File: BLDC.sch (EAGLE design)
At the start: 124 parts, among them J2 1729157, J3 1729128, Q1 IRFS7530TRLPBF, Q2 IRFS7530TRLPBF, Q3 IRFS7530TRLPBF, Q4 IRFS7530TRLPBF, Q5 IRFS7530TRLPBF, Q6 IRFS7530TRLPBF, U1 DRV8302, U102 LM3671MF-3.3/NOPB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

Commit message: Merge remote-tracking branch 'refs/remotes/origin/master'
Conflicts:
	BLDC.brd
	BLDC.sch
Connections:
- new net AGND: JP1.SHIELD
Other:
- note added: "Connect shield GND to signal GNN in one place only"
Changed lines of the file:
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@@
 <part name="P+4" library="supply1" deviceset="VCC" device=""/>
 <part name="P+5" library="supply1" deviceset="VCC" device=""/>
-<part name="GND17" library="supply1" deviceset="GND" device=""/>
 <part name="C27" library="rcl" deviceset="C-US" device="C0805" value="10uf, 50V">
 <attribute name="PARTNO" value="GRM21BR61E106KA73L"/>
@@
 <part name="GND36" library="supply1" deviceset="GND" device=""/>
 <part name="P+12" library="supply1" deviceset="+5V" device=""/>
+<part name="AGND1" library="supply1" deviceset="AGND" device=""/>
+<part name="AGND2" library="supply1" deviceset="AGND" device=""/>
+<part name="GND17" library="supply1" deviceset="GND" device=""/>
+<part name="SUPPLY1" library="supply2" deviceset="DGND" device=""/>
+<part name="SUPPLY2" library="supply2" deviceset="DGND" device=""/>
 </parts>
 <sheets>
@@
 <text x="-231.14" y="43.18" size="1.778" layer="97">INPUTS</text>
 <text x="-375.92" y="149.86" size="1.778" layer="97">USB shield?</text>
-<text x="-170.18" y="53.34" size="2.54" layer="97">USB shield?</text>
 <text x="-127" y="60.96" size="1.778" layer="97">Mount if used
 as USB Host</text>
@@
 <wire x1="43.18" y1="-241.3" x2="-106.68" y2="-241.3" width="0.6096" layer="97"/>
 <wire x1="-106.68" y1="-241.3" x2="-106.68" y2="-144.78" width="0.6096" layer="97"/>
+<text x="-177.8" y="45.72" size="1.778" layer="97">Connect shield
+GND to signal
+GNN in one
+place only</text>
 </plain>
 <instances>
@@
 <instance part="P+4" gate="VCC" x="-215.9" y="27.94" rot="R270"/>
 <instance part="P+5" gate="VCC" x="223.52" y="76.2"/>
-<instance part="GND17" gate="1" x="-215.9" y="25.4" rot="MR270"/>
 <instance part="C27" gate="G$1" x="236.22" y="66.04" rot="MR0">
 <attribute name="PARTNO" x="236.22" y="66.04" size="6.4516" layer="96" rot="MR0" display="off"/>
@@
 <instance part="GND36" gate="1" x="35.56" y="-190.5"/>
 <instance part="P+12" gate="1" x="35.56" y="-160.02"/>
+<instance part="AGND1" gate="VR1" x="-157.48" y="43.18"/>
+<instance part="AGND2" gate="VR1" x="-193.04" y="33.02"/>
+<instance part="GND17" gate="1" x="-185.42" y="33.02"/>
+<instance part="SUPPLY1" gate="G$1" x="-203.2" y="33.02"/>
+<instance part="SUPPLY2" gate="G$1" x="-215.9" y="25.4" rot="R90"/>
 </instances>
 <busses>
@@
 <wire x1="-76.2" y1="83.82" x2="-76.2" y2="81.28" width="0.1524" layer="91"/>
 <junction x="-76.2" y="81.28"/>
-</segment>
-<segment>
-<wire x1="-233.68" y1="25.4" x2="-218.44" y2="25.4" width="0.1524" layer="91"/>
-<label x="-233.68" y="25.4" size="1.778" layer="95"/>
-<pinref part="GND17" gate="1" pin="GND"/>
 </segment>
 <segment>
@@
 <segment>
 <pinref part="R4" gate="G$1" pin="1"/>
-<wire x1="-116.84" y1="45.72" x2="-104.14" y2="45.72" width="0.1524" layer="91"/>
-<label x="-114.3" y="45.72" size="1.778" layer="95"/>
+<wire x1="-116.84" y1="45.72" x2="-114.3" y2="45.72" width="0.1524" layer="91"/>
+<label x="-114.3" y="45.72" size="1.778" layer="95" xref="yes"/>
 </segment>
 </net>
@@
 <segment>
 <pinref part="R3" gate="G$1" pin="1"/>
-<wire x1="-116.84" y1="53.34" x2="-104.14" y2="53.34" width="0.1524" layer="91"/>
-<label x="-114.3" y="53.34" size="1.778" layer="95"/>
+<wire x1="-116.84" y1="53.34" x2="-114.3" y2="53.34" width="0.1524" layer="91"/>
+<label x="-114.3" y="53.34" size="1.778" layer="95" xref="yes"/>
 </segment>
 </net>
@@
 </segment>
 </net>
+<net name="AGND" class="0">
+<segment>
+<pinref part="JP1" gate="G$1" pin="SHIELD"/>
+<pinref part="AGND1" gate="VR1" pin="AGND"/>
+<wire x1="-152.4" y1="50.8" x2="-157.48" y2="50.8" width="0.1524" layer="91"/>
+<wire x1="-157.48" y1="50.8" x2="-157.48" y2="45.72" width="0.1524" layer="91"/>
+</segment>
+</net>
+<net name="DGND" class="0">
+<segment>
+<wire x1="-203.2" y1="35.56" x2="-203.2" y2="38.1" width="0.1524" layer="91"/>
+<pinref part="GND17" gate="1" pin="GND"/>
+<wire x1="-203.2" y1="38.1" x2="-193.04" y2="38.1" width="0.1524" layer="91"/>
+<wire x1="-193.04" y1="38.1" x2="-185.42" y2="38.1" width="0.1524" layer="91"/>
+<wire x1="-185.42" y1="38.1" x2="-185.42" y2="35.56" width="0.1524" layer="91"/>
+<pinref part="AGND2" gate="VR1" pin="AGND"/>
+<wire x1="-193.04" y1="35.56" x2="-193.04" y2="38.1" width="0.1524" layer="91"/>
+<junction x="-193.04" y="38.1"/>
+<pinref part="SUPPLY1" gate="G$1" pin="DGND"/>
+</segment>
+<segment>
+<wire x1="-233.68" y1="25.4" x2="-218.44" y2="25.4" width="0.1524" layer="91"/>
+<label x="-233.68" y="25.4" size="1.778" layer="95"/>
+<pinref part="SUPPLY2" gate="G$1" pin="DGND"/>
+</segment>
+</net>

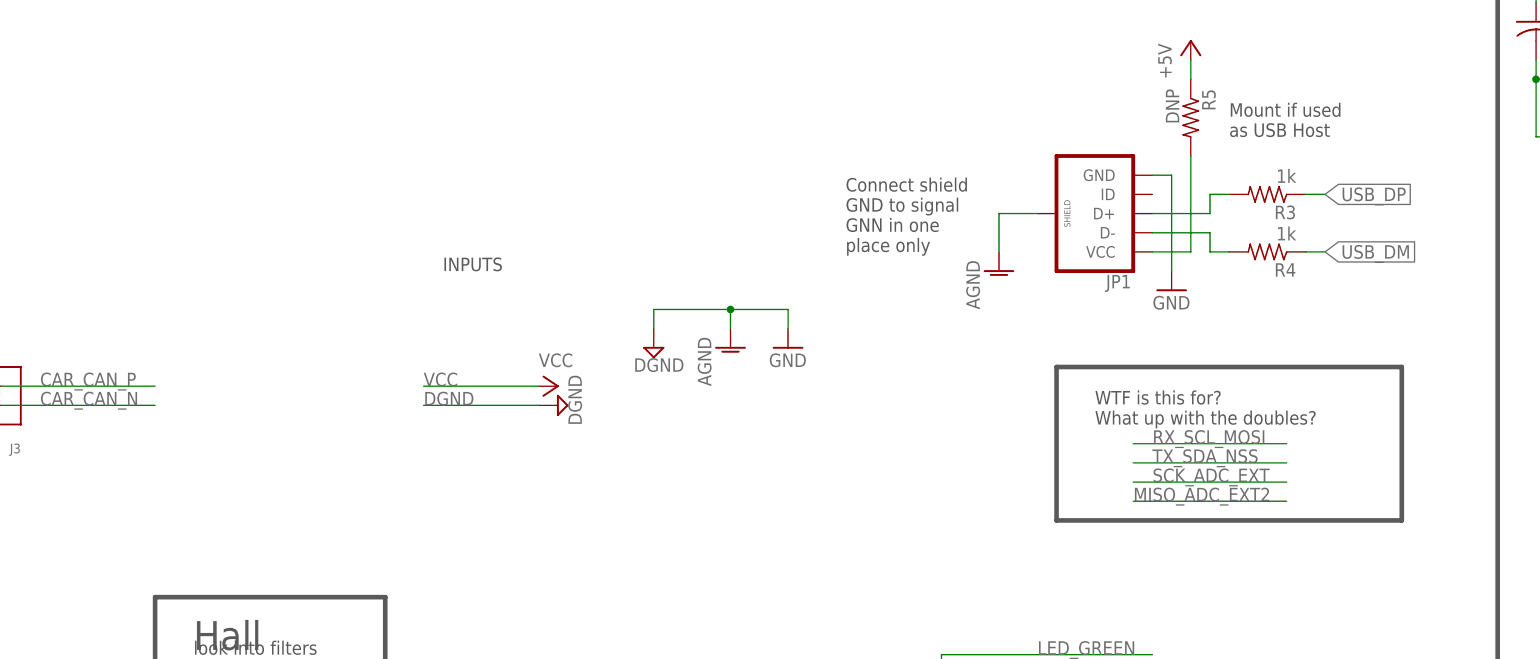
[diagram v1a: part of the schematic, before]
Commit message: added some inputs
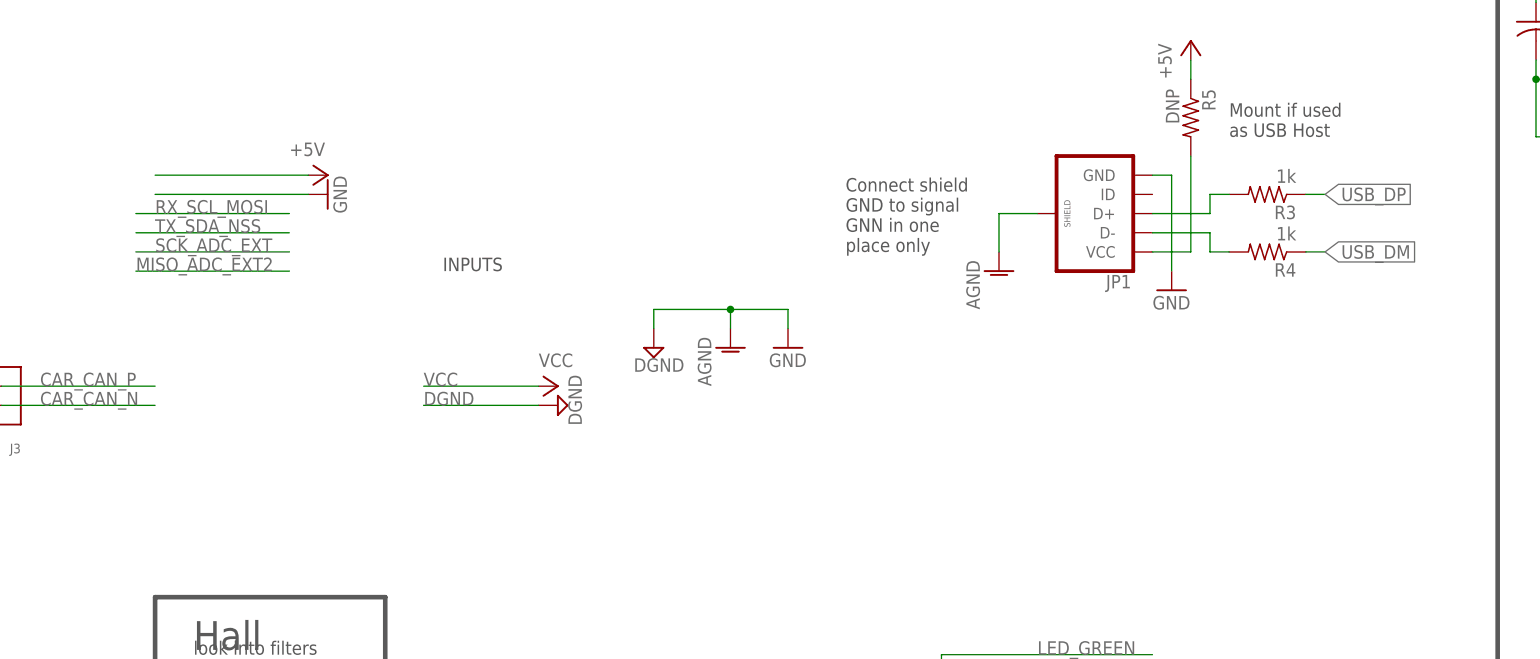
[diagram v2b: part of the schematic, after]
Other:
- note removed: "WTF is this for? What up with the doubles?"
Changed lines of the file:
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@@
 <part name="SUPPLY1" library="supply2" deviceset="DGND" device=""/>
 <part name="SUPPLY2" library="supply2" deviceset="DGND" device=""/>
+<part name="GND37" library="supply1" deviceset="GND" device=""/>
+<part name="P+13" library="supply1" deviceset="+5V" device=""/>
 </parts>
 <sheets>
@@
 Halls?</text>
 <text x="-261.62" y="203.2" size="6.4516" layer="97">BLDC-PCB</text>
-<text x="-144.78" y="22.86" size="1.778" layer="97">WTF is this for?
-What up with the doubles?</text>
-<wire x1="-149.86" y1="10.16" x2="-104.14" y2="10.16" width="0.6096" layer="97"/>
-<wire x1="-104.14" y1="10.16" x2="-104.14" y2="30.48" width="0.6096" layer="97"/>
-<wire x1="-104.14" y1="30.48" x2="-149.86" y2="30.48" width="0.6096" layer="97"/>
-<wire x1="-149.86" y1="30.48" x2="-149.86" y2="10.16" width="0.6096" layer="97"/>
 <text x="-231.14" y="43.18" size="1.778" layer="97">INPUTS</text>
 <text x="-375.92" y="149.86" size="1.778" layer="97">USB shield?</text>
@@
 <instance part="SUPPLY1" gate="G$1" x="-203.2" y="33.02"/>
 <instance part="SUPPLY2" gate="G$1" x="-215.9" y="25.4" rot="R90"/>
+<instance part="GND37" gate="1" x="-246.38" y="53.34" rot="R90"/>
+<instance part="P+13" gate="1" x="-246.38" y="55.88" rot="R270"/>
 </instances>
 <busses>
@@
 <wire x1="35.56" y1="-187.96" x2="35.56" y2="-185.42" width="0.1524" layer="91"/>
 </segment>
+<segment>
+<wire x1="-269.24" y1="53.34" x2="-248.92" y2="53.34" width="0.1524" layer="91"/>
+<pinref part="GND37" gate="1" pin="GND"/>
+</segment>
 </net>
 <net name="+5V" class="0">
@@
 <pinref part="P+12" gate="1" pin="+5V"/>
 </segment>
+<segment>
+<wire x1="-269.24" y1="55.88" x2="-248.92" y2="55.88" width="0.1524" layer="91"/>
+<pinref part="P+13" gate="1" pin="+5V"/>
+</segment>
 </net>
 <net name="+3V3" class="0">
@@
 </segment>
 <segment>
-<wire x1="-119.38" y1="20.32" x2="-139.7" y2="20.32" width="0.1524" layer="91"/>
-<label x="-137.16" y="20.32" size="1.778" layer="95"/>
+<wire x1="-251.46" y1="50.8" x2="-271.78" y2="50.8" width="0.1524" layer="91"/>
+<label x="-269.24" y="50.8" size="1.778" layer="95"/>
 </segment>
 </net>
@@
 </segment>
 <segment>
-<wire x1="-119.38" y1="15.24" x2="-139.7" y2="15.24" width="0.1524" layer="91"/>
-<label x="-137.16" y="15.24" size="1.778" layer="95"/>
+<wire x1="-251.46" y1="45.72" x2="-271.78" y2="45.72" width="0.1524" layer="91"/>
+<label x="-269.24" y="45.72" size="1.778" layer="95"/>
 </segment>
 </net>
@@
 </segment>
 <segment>
-<wire x1="-119.38" y1="17.78" x2="-139.7" y2="17.78" width="0.1524" layer="91"/>
-<label x="-137.16" y="17.78" size="1.778" layer="95"/>
+<wire x1="-251.46" y1="48.26" x2="-271.78" y2="48.26" width="0.1524" layer="91"/>
+<label x="-269.24" y="48.26" size="1.778" layer="95"/>
 </segment>
 </net>
@@
 </segment>
 <segment>
-<wire x1="-119.38" y1="12.7" x2="-139.7" y2="12.7" width="0.1524" layer="91"/>
-<label x="-139.7" y="12.7" size="1.778" layer="95"/>
-</segment>
-</net>
+<wire x1="-251.46" y1="43.18" x2="-271.78" y2="43.18" width="0.1524" layer="91"/>
+<label x="-271.78" y="43.18" size="1.778" layer="95"/>
+</segment>
+</net>

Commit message: Added note about dc-dc converter
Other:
- note added: "NEED??????"
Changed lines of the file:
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@@
 GNN in one
 place only</text>
+<text x="-58.42" y="-187.96" size="6.4516" layer="97">NEED??????</text>
 </plain>
 <instances>

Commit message: added dummy aux inputs
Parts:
- removed J2: 1729157, FormE:PHOENIX-MKDSN-5
- removed J3: 1729128, FormE:PHOENIX-MKDSN-2
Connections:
- net +3V3: no longer J2.5
- net CAR_CAN_N: no longer J3.1
- net CAR_CAN_P: no longer J3.2
- net GND: no longer J2.1
- net NRST: no longer J2.2
- net SWCLK: no longer J2.4
- net SWDIO: no longer J2.3
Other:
- note added: "NEED TO DECIDE HOW MANY AUX!!!!!!!!!!!!!!"
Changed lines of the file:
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@@
 <part name="+3V7" library="supply1" deviceset="+3V3" device=""/>
 <part name="GND26" library="supply1" deviceset="GND" device=""/>
-<part name="J2" library="FormE" deviceset="PHOENIX-MKDSN-5" device="" value="1729157"/>
-<part name="J3" library="FormE" deviceset="PHOENIX-MKDSN-2" device="" value="1729128"/>
 <part name="R40" library="FormE" deviceset="WSLP27261L000FEA" device="" value=".001R"/>
 <part name="U3" library="FormE" deviceset="LT3433" device=""/>
@@
 <part name="GND37" library="supply1" deviceset="GND" device=""/>
 <part name="P+13" library="supply1" deviceset="+5V" device=""/>
+<part name="P+15" library="supply1" deviceset="+5V" device=""/>
+<part name="GND42" library="supply1" deviceset="GND" device=""/>
 </parts>
 <sheets>
@@
 place only</text>
 <text x="-58.42" y="-187.96" size="6.4516" layer="97">NEED??????</text>
+<text x="-93.98" y="180.34" size="6.4516" layer="97">NEED TO DECIDE HOW MANY AUX!!!!!!!!!!!!!!</text>
 </plain>
 <instances>
@@
 <instance part="+3V7" gate="G$1" x="-302.26" y="78.74"/>
 <instance part="GND26" gate="1" x="-302.26" y="48.26"/>
-<instance part="J2" gate="G$1" x="-309.88" y="63.5" rot="R180"/>
-<instance part="J3" gate="G$1" x="-297.18" y="27.94" rot="R180"/>
 <instance part="R40" gate="G$1" x="320.04" y="17.78" rot="R90"/>
 <instance part="U3" gate="G$1" x="-38.1" y="-177.8"/>
@@
 <instance part="GND37" gate="1" x="-246.38" y="53.34" rot="R90"/>
 <instance part="P+13" gate="1" x="-246.38" y="55.88" rot="R270"/>
+<instance part="P+15" gate="1" x="-266.7" y="30.48" rot="R270"/>
+<instance part="GND42" gate="1" x="-266.7" y="22.86" rot="R90"/>
 </instances>
 <busses>
@@
 <wire x1="-302.26" y1="58.42" x2="-302.26" y2="50.8" width="0.1524" layer="91"/>
 <pinref part="GND26" gate="1" pin="GND"/>
-<pinref part="J2" gate="G$1" pin="1"/>
 <wire x1="-302.26" y1="58.42" x2="-307.34" y2="58.42" width="0.1524" layer="91"/>
 </segment>
@@
 <wire x1="-269.24" y1="53.34" x2="-248.92" y2="53.34" width="0.1524" layer="91"/>
 <pinref part="GND37" gate="1" pin="GND"/>
+</segment>
+<segment>
+<wire x1="-289.56" y1="22.86" x2="-269.24" y2="22.86" width="0.1524" layer="91"/>
+<pinref part="GND42" gate="1" pin="GND"/>
 </segment>
 </net>
@@
 <pinref part="P+13" gate="1" pin="+5V"/>
 </segment>
+<segment>
+<wire x1="-289.56" y1="30.48" x2="-269.24" y2="30.48" width="0.1524" layer="91"/>
+<pinref part="P+15" gate="1" pin="+5V"/>
+</segment>
 </net>
 <net name="+3V3" class="0">
@@
 <wire x1="-302.26" y1="68.58" x2="-302.26" y2="76.2" width="0.1524" layer="91"/>
 <pinref part="+3V7" gate="G$1" pin="+3V3"/>
-<pinref part="J2" gate="G$1" pin="5"/>
 <wire x1="-302.26" y1="68.58" x2="-307.34" y2="68.58" width="0.1524" layer="91"/>
 </segment>
@@
 </segment>
 <segment>
-<pinref part="J3" gate="G$1" pin="2"/>
 <wire x1="-289.56" y1="27.94" x2="-269.24" y2="27.94" width="0.1524" layer="91"/>
 <label x="-284.48" y="27.94" size="1.778" layer="95"/>
@@
 </segment>
 <segment>
-<pinref part="J3" gate="G$1" pin="1"/>
 <wire x1="-289.56" y1="25.4" x2="-269.24" y2="25.4" width="0.1524" layer="91"/>
 <label x="-284.48" y="25.4" size="1.778" layer="95"/>
@@
 <segment>
 <label x="-302.26" y="66.04" size="1.778" layer="95"/>
-<pinref part="J2" gate="G$1" pin="4"/>
 <wire x1="-294.64" y1="66.04" x2="-307.34" y2="66.04" width="0.1524" layer="91"/>
 </segment>
@@
 <segment>
 <label x="-302.26" y="63.5" size="1.778" layer="95"/>
-<pinref part="J2" gate="G$1" pin="3"/>
 <wire x1="-294.64" y1="63.5" x2="-307.34" y2="63.5" width="0.1524" layer="91"/>
 </segment>
@@
 <segment>
 <label x="-302.26" y="60.96" size="1.778" layer="95"/>
-<pinref part="J2" gate="G$1" pin="2"/>
 <wire x1="-294.64" y1="60.96" x2="-307.34" y2="60.96" width="0.1524" layer="91"/>
 </segment>
@@
 </segment>
 </net>
+<net name="AUX_1" class="0">
+<segment>
+<wire x1="-264.16" y1="73.66" x2="-243.84" y2="73.66" width="0.1524" layer="91"/>
+<label x="-264.16" y="73.66" size="1.778" layer="95"/>
+</segment>
+</net>
+<net name="AUX_2" class="0">
+<segment>
+<wire x1="-264.16" y1="71.12" x2="-243.84" y2="71.12" width="0.1524" layer="91"/>
+<label x="-264.16" y="71.12" size="1.778" layer="95"/>
+</segment>
+</net>
+<net name="AUX_3" class="0">
+<segment>
+<wire x1="-264.16" y1="68.58" x2="-243.84" y2="68.58" width="0.1524" layer="91"/>
+<label x="-264.16" y="68.58" size="1.778" layer="95"/>
+</segment>
+</net>
+<net name="AUX_4" class="0">
+<segment>
+<wire x1="-264.16" y1="66.04" x2="-243.84" y2="66.04" width="0.1524" layer="91"/>
+<label x="-264.16" y="66.04" size="1.778" layer="95"/>
+</segment>
+</net>
+<net name="AUX_5" class="0">
+<segment>
+<wire x1="-264.16" y1="63.5" x2="-243.84" y2="63.5" width="0.1524" layer="91"/>
+<label x="-264.16" y="63.5" size="1.778" layer="95"/>
+</segment>
+</net>
+<net name="AUX_6" class="0">
+<segment>
+<wire x1="-264.16" y1="60.96" x2="-243.84" y2="60.96" width="0.1524" layer="91"/>
+<label x="-264.16" y="60.96" size="1.778" layer="95"/>
+</segment>
+</net>
